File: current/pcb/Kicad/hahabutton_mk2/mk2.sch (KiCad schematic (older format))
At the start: 29 parts, among them U1 SAMB11G18A, Y1 32.768kHz, Y2 26MHz

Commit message: work on MIFA footprint begins...
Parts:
- C?: footprint (none) -> Capacitors_SMD:C_0805
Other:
- moved on the sheet: BT?, C?, D?
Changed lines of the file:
@@
 	1    0    0    -1
 $EndComp
-Text Label 8600 2400 1    60   ~ 0
+Text Label 7100 2950 1    60   ~ 0
 +3.0V
 $Comp
 L Battery_Cell BT?
 U 1 1 5A4290BB
-P 8600 2900
-F 0 "BT?" H 8700 3000 50  0000 L CNN
-F 1 "Battery_Cell" H 8700 2900 50  0000 L CNN
-F 2 "" V 8600 2960 50  0000 C CNN
-F 3 "" V 8600 2960 50  0000 C CNN
-	1    8600 2900
+P 7100 3450
+F 0 "BT?" H 7200 3550 50  0000 L CNN
+F 1 "Battery_Cell" H 7200 3450 50  0000 L CNN
+F 2 "" V 7100 3510 50  0000 C CNN
+F 3 "" V 7100 3510 50  0000 C CNN
+	1    7100 3450
 	1    0    0    -1
 $EndComp
@@
 L D_Schottky D?
 U 1 1 5A4291B5
-P 8600 2550
-F 0 "D?" V 8650 2100 50  0000 C CNN
-F 1 "D_Schottky" V 8550 2250 50  0000 C CNN
-F 2 "" H 8600 2550 50  0000 C CNN
-F 3 "" H 8600 2550 50  0000 C CNN
-	1    8600 2550
+P 7100 3100
+F 0 "D?" V 7150 2650 50  0000 C CNN
+F 1 "D_Schottky" V 7050 2800 50  0000 C CNN
+F 2 "" H 7100 3100 50  0000 C CNN
+F 3 "" H 7100 3100 50  0000 C CNN
+	1    7100 3100
 	0    1    1    0
 $EndComp
@@
 L CP C?
 U 1 1 5A429414
-P 9300 2850
-F 0 "C?" H 9325 2950 50  0000 L CNN
-F 1 "CP" H 9325 2750 50  0000 L CNN
-F 2 "" H 9338 2700 50  0000 C CNN
-F 3 "" H 9300 2850 50  0000 C CNN
-	1    9300 2850
+P 7800 3400
+F 0 "C?" H 7825 3500 50  0000 L CNN
+F 1 "CP" H 7825 3300 50  0000 L CNN
+F 2 "Capacitors_SMD:C_0805" H 7838 3250 50  0001 C CNN
+F 3 "" H 7800 3400 50  0000 C CNN
+	1    7800 3400
 	1    0    0    -1
 $EndComp
 Wire Wire Line
-	8600 2700 9300 2700
+	7100 3250 7800 3250
 Wire Wire Line
-	9300 3000 8600 3000
+	7800 3550 7100 3550
 $Comp
 L GND #PWR?
 U 1 1 5A42961E
-P 8600 3000
-F 0 "#PWR?" H 8600 2750 50  0001 C CNN
-F 1 "GND" H 8600 2875 50  0000 C CNN
-F 2 "" H 8600 3000 50  0000 C CNN
-F 3 "" H 8600 3000 50  0000 C CNN
-	1    8600 3000
+P 7100 3550
+F 0 "#PWR?" H 7100 3300 50  0001 C CNN
+F 1 "GND" H 7100 3425 50  0000 C CNN
+F 2 "" H 7100 3550 50  0000 C CNN
+F 3 "" H 7100 3550 50  0000 C CNN
+	1    7100 3550
 	1    0    0    -1
 $EndComp

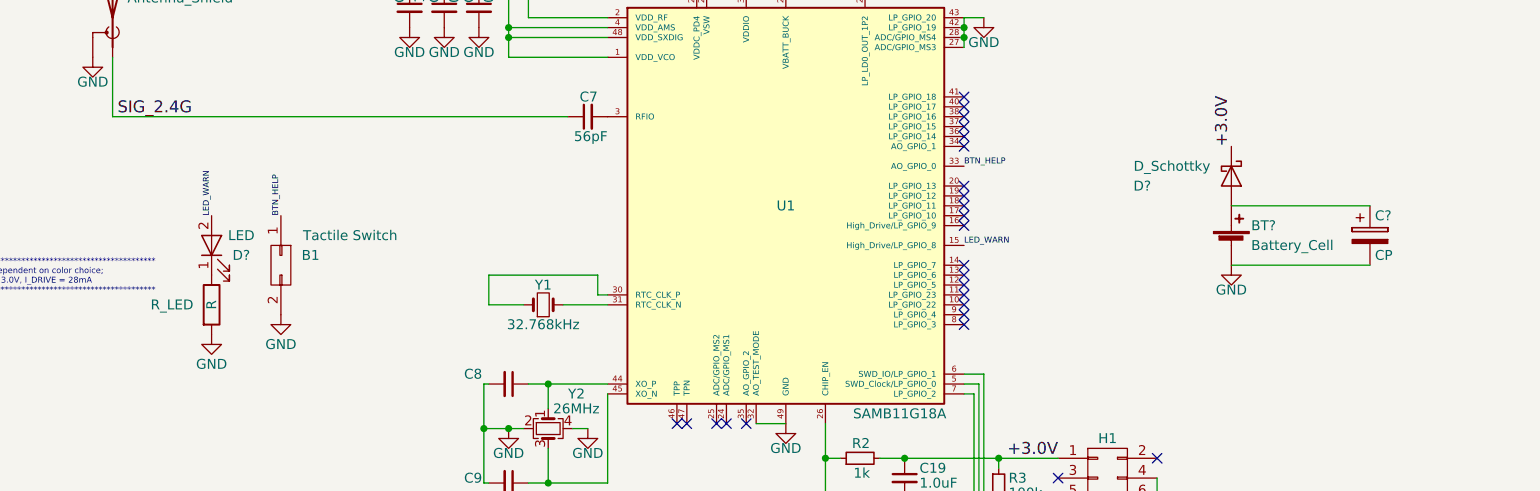
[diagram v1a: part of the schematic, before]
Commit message: antenna stencil made; began layout.
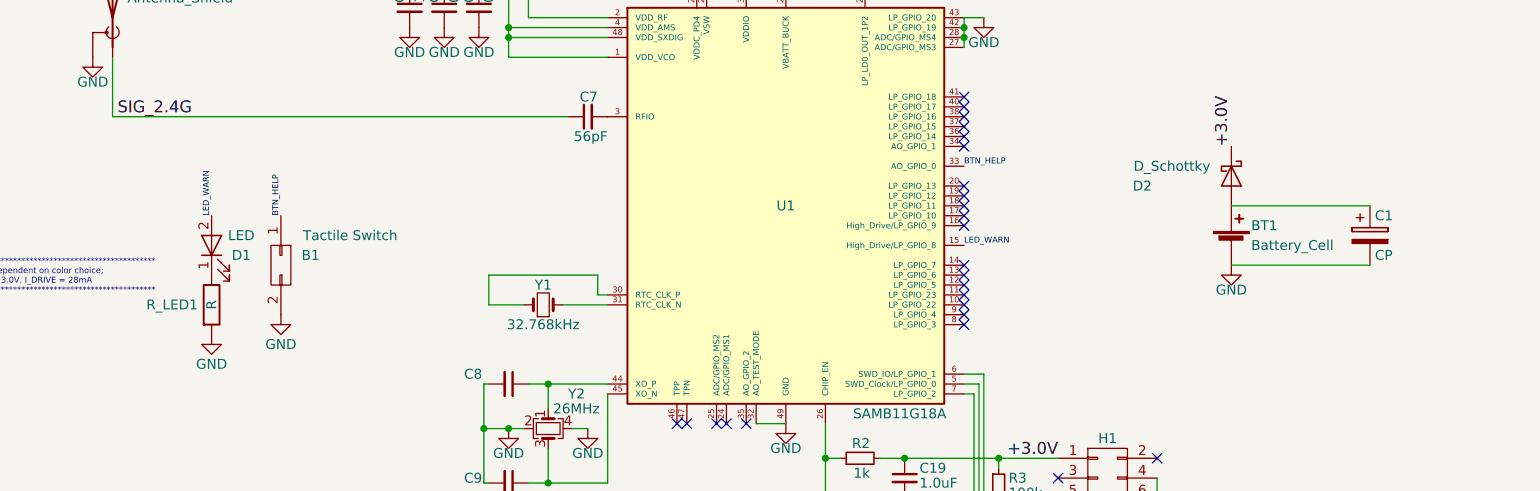
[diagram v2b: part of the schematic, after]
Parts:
- AE1: footprint Antennas:Patch_Antenna_2.4GHz -> Antennas:2p4GHzMIFA_cust
- gave numbers to parts that had none: 4
- renumbered R_LED to R_LED1
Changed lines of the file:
@@
 Base
 $Comp
-L GND #PWR01
+L GND #PWR12
 U 1 1 58BA111C
 P 4850 4350
-F 0 "#PWR01" H 4850 4100 50  0001 C CNN
+F 0 "#PWR12" H 4850 4100 50  0001 C CNN
 F 1 "GND" H 4850 4225 50  0000 C CNN
 F 2 "" H 4850 4350 50  0000 C CNN
@@
 NoConn ~ 6225 5325
 $Comp
-L GND #PWR02
+L GND #PWR18
 U 1 1 58BBBCA3
 P 6725 5425
-F 0 "#PWR02" H 6725 5175 50  0001 C CNN
+F 0 "#PWR18" H 6725 5175 50  0001 C CNN
 F 1 "GND" H 6725 5300 50  0000 C CNN
 F 2 "" H 6725 5425 50  0000 C CNN
@@
 $EndComp
 $Comp
-L GND #PWR03
+L GND #PWR13
 U 1 1 58BB38DF
 P 4950 2025
-F 0 "#PWR03" H 4950 1775 50  0001 C CNN
+F 0 "#PWR13" H 4950 1775 50  0001 C CNN
 F 1 "GND" H 4950 1900 50  0000 C CNN
 F 2 "" H 4950 2025 50  0000 C CNN
@@
 $EndComp
 $Comp
-L GND #PWR04
+L GND #PWR14
 U 1 1 58BB3BF8
 P 5125 2025
-F 0 "#PWR04" H 5125 1775 50  0001 C CNN
+F 0 "#PWR14" H 5125 1775 50  0001 C CNN
 F 1 "GND" H 5125 1900 50  0000 C CNN
 F 2 "" H 5125 2025 50  0000 C CNN
@@
 $EndComp
 $Comp
-L GND #PWR05
+L GND #PWR15
 U 1 1 58BB3E12
 P 5350 2025
-F 0 "#PWR05" H 5350 1775 50  0001 C CNN
+F 0 "#PWR15" H 5350 1775 50  0001 C CNN
 F 1 "GND" H 5350 1900 50  0000 C CNN
 F 2 "" H 5350 2025 50  0000 C CNN
@@
 $EndComp
 $Comp
-L GND #PWR06
+L GND #PWR11
 U 1 1 58BB3E50
 P 4750 2025
-F 0 "#PWR06" H 4750 1775 50  0001 C CNN
+F 0 "#PWR11" H 4750 1775 50  0001 C CNN
 F 1 "GND" H 4750 1900 50  0000 C CNN
 F 2 "" H 4750 2025 50  0000 C CNN
@@
 $EndComp
 $Comp
-L GND #PWR07
+L GND #PWR10
 U 1 1 58BB7D62
 P 4550 2025
-F 0 "#PWR07" H 4550 1775 50  0001 C CNN
+F 0 "#PWR10" H 4550 1775 50  0001 C CNN
 F 1 "GND" H 4550 1900 50  0000 C CNN
 F 2 "" H 4550 2025 50  0000 C CNN
@@
 $EndComp
 $Comp
-L GND #PWR08
+L GND #PWR8
 U 1 1 58BC1891
 P 3650 2050
-F 0 "#PWR08" H 3650 1800 50  0001 C CNN
+F 0 "#PWR8" H 3650 1800 50  0001 C CNN
 F 1 "GND" H 3650 1925 50  0000 C CNN
 F 2 "" H 3650 2050 50  0000 C CNN
@@
 $EndComp
 $Comp
-L GND #PWR09
+L GND #PWR6
 U 1 1 58BCD298
 P 3300 2350
-F 0 "#PWR09" H 3300 2100 50  0001 C CNN
+F 0 "#PWR6" H 3300 2100 50  0001 C CNN
 F 1 "GND" H 3300 2225 50  0000 C CNN
 F 2 "" H 3300 2350 50  0000 C CNN
@@
 $EndComp
 $Comp
-L GND #PWR010
+L GND #PWR5
 U 1 1 58BCD310
 P 3125 2350
-F 0 "#PWR010" H 3125 2100 50  0001 C CNN
+F 0 "#PWR5" H 3125 2100 50  0001 C CNN
 F 1 "GND" H 3125 2225 50  0000 C CNN
 F 2 "" H 3125 2350 50  0000 C CNN
@@
 $EndComp
 $Comp
-L GND #PWR011
+L GND #PWR4
 U 1 1 58BCD378
 P 2950 2350
-F 0 "#PWR011" H 2950 2100 50  0001 C CNN
+F 0 "#PWR4" H 2950 2100 50  0001 C CNN
 F 1 "GND" H 2950 2225 50  0000 C CNN
 F 2 "" H 2950 2350 50  0000 C CNN
@@
 $EndComp
 $Comp
-L GND #PWR012
+L GND #PWR16
 U 1 1 58BE1A8E
 P 5450 4725
-F 0 "#PWR012" H 5450 4475 50  0001 C CNN
+F 0 "#PWR16" H 5450 4475 50  0001 C CNN
 F 1 "GND" H 5450 4600 50  0000 C CNN
 F 2 "" H 5450 4725 50  0000 C CNN
@@
 $EndComp
 $Comp
-L GND #PWR013
+L GND #PWR9
 U 1 1 58BE3DF0
 P 3850 4375
-F 0 "#PWR013" H 3850 4125 50  0001 C CNN
+F 0 "#PWR9" H 3850 4125 50  0001 C CNN
 F 1 "GND" H 3850 4250 50  0000 C CNN
 F 2 "" H 3850 4375 50  0000 C CNN
@@
 $EndComp
 $Comp
-L GND #PWR014
+L GND #PWR7
 U 1 1 58BE3F81
 P 3450 4375
-F 0 "#PWR014" H 3450 4125 50  0001 C CNN
+F 0 "#PWR7" H 3450 4125 50  0001 C CNN
 F 1 "GND" H 3450 4250 50  0000 C CNN
 F 2 "" H 3450 4375 50  0000 C CNN
@@
 F 0 "AE1" H 1375 2475 50  0000 R CNN
 F 1 "Antenna_Shield" H 1375 2400 50  0000 R CNN
-F 2 "Antennas:Patch_Antenna_2.4GHz" H 1450 2400 50  0001 C CNN
+F 2 "Antennas:2p4GHzMIFA_cust" H 1450 2400 50  0001 C CNN
 F 3 "" H 1450 2400 50  0001 C CNN
 	1    1450 2300
@@
 $EndComp
 $Comp
-L GND #PWR015
+L GND #PWR1
 U 1 1 58E322FD
 P 1350 2500
-F 0 "#PWR015" H 1350 2250 50  0001 C CNN
+F 0 "#PWR1" H 1350 2250 50  0001 C CNN
 F 1 "GND" H 1350 2375 50  0000 C CNN
 F 2 "" H 1350 2500 50  0000 C CNN
@@
 BTN_HELP
 $Comp
-L GND #PWR016
+L GND #PWR3
 U 1 1 58EA125A
 P 2300 3800
-F 0 "#PWR016" H 2300 3550 50  0001 C CNN
+F 0 "#PWR3" H 2300 3550 50  0001 C CNN
 F 1 "GND" H 2300 3650 50  0000 C CNN
 F 2 "" H 2300 3800 50  0000 C CNN
@@
 +3.0V
 $Comp
-L GND #PWR017
+L GND #PWR17
 U 1 1 590F9EAC
 P 5850 2300
-F 0 "#PWR017" H 5850 2050 50  0001 C CNN
+F 0 "#PWR17" H 5850 2050 50  0001 C CNN
 F 1 "GND" H 5850 2175 50  0000 C CNN
 F 2 "" H 5850 2300 50  0000 C CNN
@@
 	4700 4350 4850 4350
 $Comp
-L LED D?
+L LED D1
 U 1 1 5A33776E
 P 1950 3450
-F 0 "D?" V 1900 3300 50  0000 C CNN
+F 0 "D1" V 1900 3300 50  0000 C CNN
 F 1 "LED" V 2000 3300 50  0000 C CNN
 F 2 "LEDs:LED_0402_1005Metric" H 1950 3450 50  0001 C CNN
@@
 $EndComp
 $Comp
-L R R_LED
+L R R_LED1
 U 1 1 5A33890A
 P 1950 3750
-F 0 "R_LED" H 1750 3750 50  0000 C CNN
+F 0 "R_LED1" H 1750 3750 50  0000 C CNN
 F 1 "R" V 1950 3750 50  0000 C CNN
 F 2 "Capacitors_SMD:C_0402" V 1880 3750 50  0001 C CNN
@@
 $EndComp
 $Comp
-L GND #PWR018
+L GND #PWR2
 U 1 1 5A33897E
 P 1950 3900
-F 0 "#PWR018" H 1950 3650 50  0001 C CNN
+F 0 "#PWR2" H 1950 3650 50  0001 C CNN
 F 1 "GND" H 1950 3750 50  0000 C CNN
 F 2 "" H 1950 3900 50  0000 C CNN
@@
 +3.0V
 $Comp
-L Battery_Cell BT?
+L Battery_Cell BT1
 U 1 1 5A4290BB
 P 7100 3450
-F 0 "BT?" H 7200 3550 50  0000 L CNN
+F 0 "BT1" H 7200 3550 50  0000 L CNN
 F 1 "Battery_Cell" H 7200 3450 50  0000 L CNN
 F 2 "" V 7100 3510 50  0000 C CNN
@@
 $EndComp
 $Comp
-L D_Schottky D?
+L D_Schottky D2
 U 1 1 5A4291B5
 P 7100 3100
-F 0 "D?" V 7150 2650 50  0000 C CNN
+F 0 "D2" V 7150 2650 50  0000 C CNN
 F 1 "D_Schottky" V 7050 2800 50  0000 C CNN
 F 2 "" H 7100 3100 50  0000 C CNN
@@
 $EndComp
 $Comp
-L CP C?
+L CP C1
 U 1 1 5A429414
 P 7800 3400
-F 0 "C?" H 7825 3500 50  0000 L CNN
+F 0 "C1" H 7825 3500 50  0000 L CNN
 F 1 "CP" H 7825 3300 50  0000 L CNN
 F 2 "Capacitors_SMD:C_0805" H 7838 3250 50  0001 C CNN
@@
 	7800 3550 7100 3550
 $Comp
-L GND #PWR?
+L GND #PWR19
 U 1 1 5A42961E
 P 7100 3550
-F 0 "#PWR?" H 7100 3300 50  0001 C CNN
+F 0 "#PWR19" H 7100 3300 50  0001 C CNN
 F 1 "GND" H 7100 3425 50  0000 C CNN
 F 2 "" H 7100 3550 50  0000 C CNN

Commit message: taking form, mkii...
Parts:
- BT1: footprint (none) -> Batteries:batt_holder3035
- D2: footprint (none) -> Diodes:D_0402_1005Metric
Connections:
- net SIG_2.4G is gone; now on net GND: AE1.1 (A), C7.1
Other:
- note added: "** Place SWD connector on seperate [removeable] module?"
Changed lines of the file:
@@
 Text Notes 5750 2075 0    60   ~ 0
 LP_GPIO_3, 4, 5, 22, 23 configured\nwith internal pull-up resistors.\nAll other GPIOs configured\nwith internal pull-down resistors.
-$Comp
-L CONN_02X10 H1
-U 1 1 58BBB586
-P 6475 4975
-F 0 "H1" H 6475 5525 50  0000 C CNN
-F 1 "J-Link SWD" V 6475 4975 50  0000 C CNN
-F 2 "Misc:Socket_Strip_Straight_2x10_Pitch2.54mm_Drill0.889mm" H 6475 3775 50  0001 C CNN
-F 3 "" H 6475 3775 50  0000 C CNN
-	1    6475 4975
-	1    0    0    -1
-$EndComp
 Text Label 6000 4825 0    30   ~ 0
 SWDIO
@@
 F 0 "BT1" H 7200 3550 50  0000 L CNN
 F 1 "Battery_Cell" H 7200 3450 50  0000 L CNN
-F 2 "" V 7100 3510 50  0000 C CNN
+F 2 "Batteries:batt_holder3035" H 7100 3510 50  0001 C CNN
 F 3 "" V 7100 3510 50  0000 C CNN
 	1    7100 3450
@@
 F 0 "D2" V 7150 2650 50  0000 C CNN
 F 1 "D_Schottky" V 7050 2800 50  0000 C CNN
-F 2 "" H 7100 3100 50  0000 C CNN
+F 2 "Diodes:D_0402_1005Metric" H 7100 3100 50  0001 C CNN
 F 3 "" H 7100 3100 50  0000 C CNN
 	1    7100 3100
@@
 	1    0    0    -1
 $EndComp
+$Comp
+L CONN_02X10 H1
+U 1 1 58BBB586
+P 6475 4975
+F 0 "H1" H 6475 5525 50  0000 C CNN
+F 1 "J-Link SWD" V 6475 4975 50  0000 C CNN
+F 2 "Misc:Socket_Strip_Straight_2x10_Pitch2.54mm_Drill0.889mm" H 6475 3775 50  0001 C CNN
+F 3 "" H 6475 3775 50  0000 C CNN
+	1    6475 4975
+	1    0    0    -1
+$EndComp
+Text Notes 6400 4300 0    30   ~ 0
+** Place SWD connector on seperate [removeable] module?
+Wire Wire Line
+	1450 2500 1350 2500
 $EndSCHEMATC

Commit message: not much change...
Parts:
- D1: footprint LEDs:LED_0402_1005Metric -> LEDs:LED_0402
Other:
- note added: "*************************************************\nNOTE:\n Footprints used must take into account the \n method of PCB assembly, namely hand- \n soldering or electrical skilleting with solder-\n paste.\n*************************************************"
- note added: "1.9"
- note added: "Button, mkii"
- note added: "January 13th, 2018"
- note removed: "1.1"
- note removed: "Base"
- note removed: "May 26, 2017"
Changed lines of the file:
@@
 $EndDescr
 Text Notes 7350 7500 0    60   ~ 0
-Base
-$Comp
-L GND #PWR12
+Button, mkii
+$Comp
+L GND #PWR01
 U 1 1 58BA111C
 P 4850 4350
-F 0 "#PWR12" H 4850 4100 50  0001 C CNN
+F 0 "#PWR01" H 4850 4100 50  0001 C CNN
 F 1 "GND" H 4850 4225 50  0000 C CNN
 F 2 "" H 4850 4350 50  0000 C CNN
@@
 NoConn ~ 6225 5325
 $Comp
-L GND #PWR18
+L GND #PWR02
 U 1 1 58BBBCA3
 P 6725 5425
-F 0 "#PWR18" H 6725 5175 50  0001 C CNN
+F 0 "#PWR02" H 6725 5175 50  0001 C CNN
 F 1 "GND" H 6725 5300 50  0000 C CNN
 F 2 "" H 6725 5425 50  0000 C CNN
@@
 $EndComp
 $Comp
-L GND #PWR13
+L GND #PWR03
 U 1 1 58BB38DF
 P 4950 2025
-F 0 "#PWR13" H 4950 1775 50  0001 C CNN
+F 0 "#PWR03" H 4950 1775 50  0001 C CNN
 F 1 "GND" H 4950 1900 50  0000 C CNN
 F 2 "" H 4950 2025 50  0000 C CNN
@@
 $EndComp
 $Comp
-L GND #PWR14
+L GND #PWR04
 U 1 1 58BB3BF8
 P 5125 2025
-F 0 "#PWR14" H 5125 1775 50  0001 C CNN
+F 0 "#PWR04" H 5125 1775 50  0001 C CNN
 F 1 "GND" H 5125 1900 50  0000 C CNN
 F 2 "" H 5125 2025 50  0000 C CNN
@@
 $EndComp
 $Comp
-L GND #PWR15
+L GND #PWR05
 U 1 1 58BB3E12
 P 5350 2025
-F 0 "#PWR15" H 5350 1775 50  0001 C CNN
+F 0 "#PWR05" H 5350 1775 50  0001 C CNN
 F 1 "GND" H 5350 1900 50  0000 C CNN
 F 2 "" H 5350 2025 50  0000 C CNN
@@
 $EndComp
 $Comp
-L GND #PWR11
+L GND #PWR06
 U 1 1 58BB3E50
 P 4750 2025
-F 0 "#PWR11" H 4750 1775 50  0001 C CNN
+F 0 "#PWR06" H 4750 1775 50  0001 C CNN
 F 1 "GND" H 4750 1900 50  0000 C CNN
 F 2 "" H 4750 2025 50  0000 C CNN
@@
 $EndComp
 $Comp
-L GND #PWR10
+L GND #PWR07
 U 1 1 58BB7D62
 P 4550 2025
-F 0 "#PWR10" H 4550 1775 50  0001 C CNN
+F 0 "#PWR07" H 4550 1775 50  0001 C CNN
 F 1 "GND" H 4550 1900 50  0000 C CNN
 F 2 "" H 4550 2025 50  0000 C CNN
@@
 $EndComp
 $Comp
-L GND #PWR8
+L GND #PWR08
 U 1 1 58BC1891
 P 3650 2050
-F 0 "#PWR8" H 3650 1800 50  0001 C CNN
+F 0 "#PWR08" H 3650 1800 50  0001 C CNN
 F 1 "GND" H 3650 1925 50  0000 C CNN
 F 2 "" H 3650 2050 50  0000 C CNN
@@
 $EndComp
 $Comp
-L GND #PWR6
+L GND #PWR09
 U 1 1 58BCD298
 P 3300 2350
-F 0 "#PWR6" H 3300 2100 50  0001 C CNN
+F 0 "#PWR09" H 3300 2100 50  0001 C CNN
 F 1 "GND" H 3300 2225 50  0000 C CNN
 F 2 "" H 3300 2350 50  0000 C CNN
@@
 $EndComp
 $Comp
-L GND #PWR5
+L GND #PWR010
 U 1 1 58BCD310
 P 3125 2350
-F 0 "#PWR5" H 3125 2100 50  0001 C CNN
+F 0 "#PWR010" H 3125 2100 50  0001 C CNN
 F 1 "GND" H 3125 2225 50  0000 C CNN
 F 2 "" H 3125 2350 50  0000 C CNN
@@
 $EndComp
 $Comp
-L GND #PWR4
+L GND #PWR011
 U 1 1 58BCD378
 P 2950 2350
-F 0 "#PWR4" H 2950 2100 50  0001 C CNN
+F 0 "#PWR011" H 2950 2100 50  0001 C CNN
 F 1 "GND" H 2950 2225 50  0000 C CNN
 F 2 "" H 2950 2350 50  0000 C CNN
@@
 $EndComp
 $Comp
-L GND #PWR16
+L GND #PWR012
 U 1 1 58BE1A8E
 P 5450 4725
-F 0 "#PWR16" H 5450 4475 50  0001 C CNN
+F 0 "#PWR012" H 5450 4475 50  0001 C CNN
 F 1 "GND" H 5450 4600 50  0000 C CNN
 F 2 "" H 5450 4725 50  0000 C CNN
@@
 $EndComp
 $Comp
-L GND #PWR9
+L GND #PWR013
 U 1 1 58BE3DF0
 P 3850 4375
-F 0 "#PWR9" H 3850 4125 50  0001 C CNN
+F 0 "#PWR013" H 3850 4125 50  0001 C CNN
 F 1 "GND" H 3850 4250 50  0000 C CNN
 F 2 "" H 3850 4375 50  0000 C CNN
@@
 $EndComp
 $Comp
-L GND #PWR7
+L GND #PWR014
 U 1 1 58BE3F81
 P 3450 4375
-F 0 "#PWR7" H 3450 4125 50  0001 C CNN
+F 0 "#PWR014" H 3450 4125 50  0001 C CNN
 F 1 "GND" H 3450 4250 50  0000 C CNN
 F 2 "" H 3450 4375 50  0000 C CNN
@@
 $EndComp
 $Comp
-L GND #PWR1
+L GND #PWR015
 U 1 1 58E322FD
 P 1350 2500
-F 0 "#PWR1" H 1350 2250 50  0001 C CNN
+F 0 "#PWR015" H 1350 2250 50  0001 C CNN
 F 1 "GND" H 1350 2375 50  0000 C CNN
 F 2 "" H 1350 2500 50  0000 C CNN
@@
 BTN_HELP
 $Comp
-L GND #PWR3
+L GND #PWR016
 U 1 1 58EA125A
 P 2300 3800
-F 0 "#PWR3" H 2300 3550 50  0001 C CNN
+F 0 "#PWR016" H 2300 3550 50  0001 C CNN
 F 1 "GND" H 2300 3650 50  0000 C CNN
 F 2 "" H 2300 3800 50  0000 C CNN
@@
 RESET
 Text Notes 8150 7650 0    60   ~ 0
-May 26, 2017
+January 13th, 2018
 Text Notes 10600 7650 0    60   ~ 0
-1.1
+1.9
 Text Label 6225 4525 2    60   ~ 0
 +3.0V
@@
 +3.0V
 $Comp
-L GND #PWR17
+L GND #PWR017
 U 1 1 590F9EAC
 P 5850 2300
-F 0 "#PWR17" H 5850 2050 50  0001 C CNN
+F 0 "#PWR017" H 5850 2050 50  0001 C CNN
 F 1 "GND" H 5850 2175 50  0000 C CNN
 F 2 "" H 5850 2300 50  0000 C CNN
@@
 F 0 "D1" V 1900 3300 50  0000 C CNN
 F 1 "LED" V 2000 3300 50  0000 C CNN
-F 2 "LEDs:LED_0402_1005Metric" H 1950 3450 50  0001 C CNN
+F 2 "LEDs:LED_0402" H 1950 3450 50  0001 C CNN
 F 3 "" H 1950 3450 50  0000 C CNN
 	1    1950 3450
@@
 $EndComp
 $Comp
-L GND #PWR2
+L GND #PWR018
 U 1 1 5A33897E
 P 1950 3900
-F 0 "#PWR2" H 1950 3650 50  0001 C CNN
+F 0 "#PWR018" H 1950 3650 50  0001 C CNN
 F 1 "GND" H 1950 3750 50  0000 C CNN
 F 2 "" H 1950 3900 50  0000 C CNN
@@
 	7800 3550 7100 3550
 $Comp
-L GND #PWR19
+L GND #PWR019
 U 1 1 5A42961E
 P 7100 3550
-F 0 "#PWR19" H 7100 3300 50  0001 C CNN
+F 0 "#PWR019" H 7100 3300 50  0001 C CNN
 F 1 "GND" H 7100 3425 50  0000 C CNN
 F 2 "" H 7100 3550 50  0000 C CNN
@@
 Wire Wire Line
 	1450 2500 1350 2500
+Text Notes 5400 7750 0    40   ~ 0
+*************************************************\nNOTE:\n Footprints used must take into account the \n method of PCB assembly, namely hand-      \n soldering or electrical skilleting with solder-\n paste.\n*************************************************
 $EndSCHEMATC

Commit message: fixed footprint paths; the progression to 2.0 continues...
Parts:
- D2: footprint Diodes:D_0402_1005Metric -> Diodes_SMD:D_0603
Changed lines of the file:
@@
 F 0 "D2" V 7150 2650 50  0000 C CNN
 F 1 "D_Schottky" V 7050 2800 50  0000 C CNN
-F 2 "Diodes:D_0402_1005Metric" H 7100 3100 50  0001 C CNN
+F 2 "Diodes_SMD:D_0603" H 7100 3100 50  0001 C CNN
 F 3 "" H 7100 3100 50  0000 C CNN
 	1    7100 3100
